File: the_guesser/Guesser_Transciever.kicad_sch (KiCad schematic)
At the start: 51 parts, among them J2 Conn_Coaxial, J3 BMI-S-209-F, U2 CC1101RGPR, U3 CC1190RGVR, U4 B39921B3728U410, X1 STDCRG2-27M

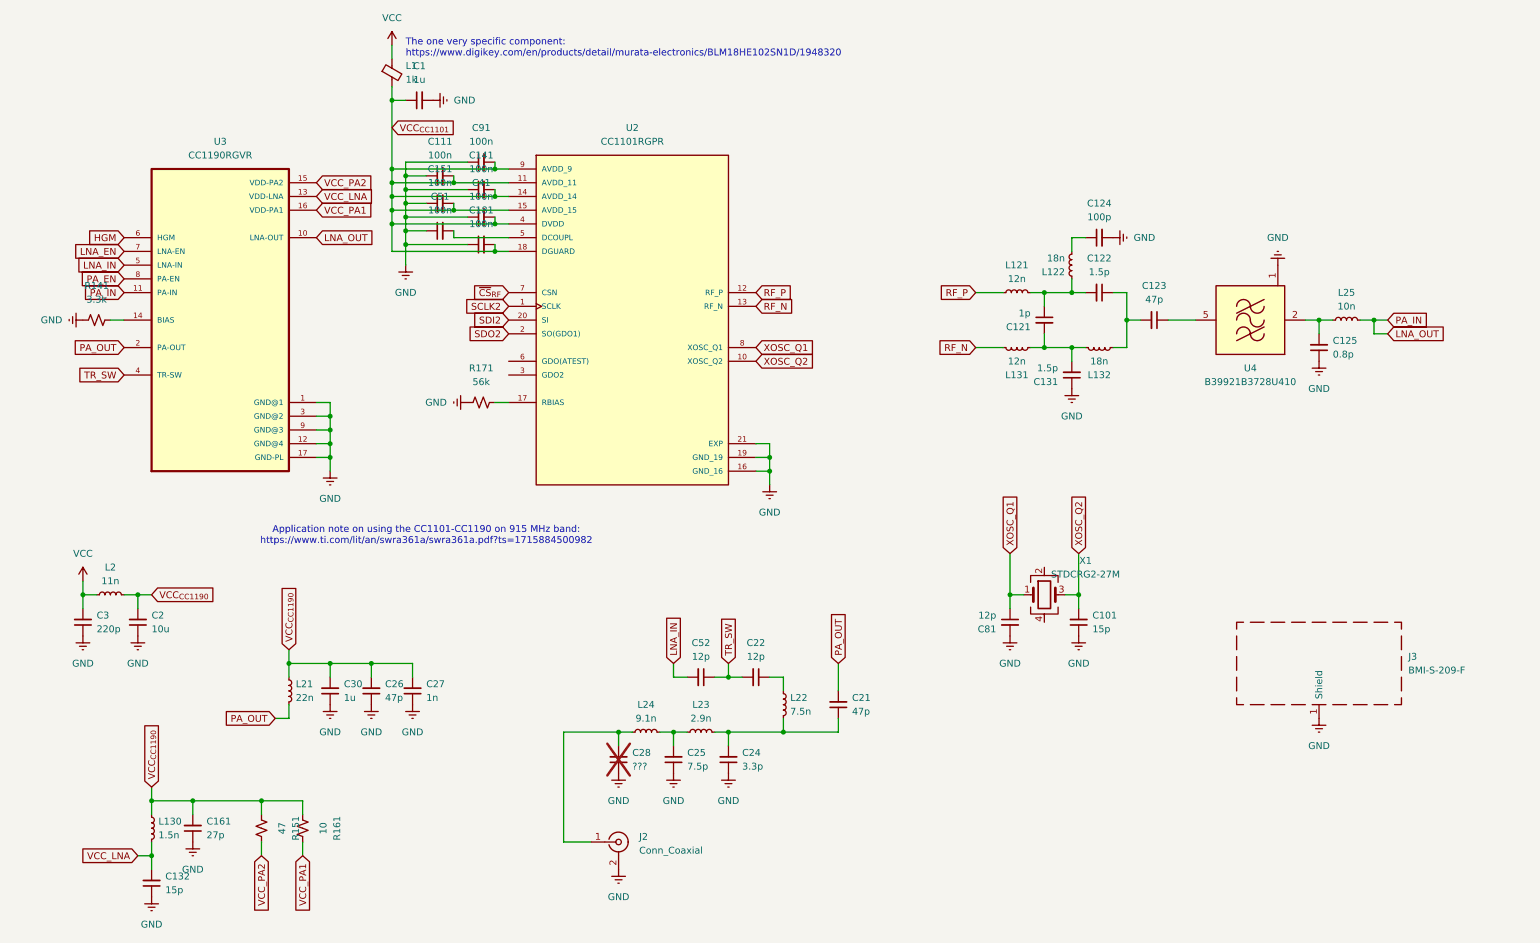
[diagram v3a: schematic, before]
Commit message: Finished Guesser sensor selection and started sensor routing
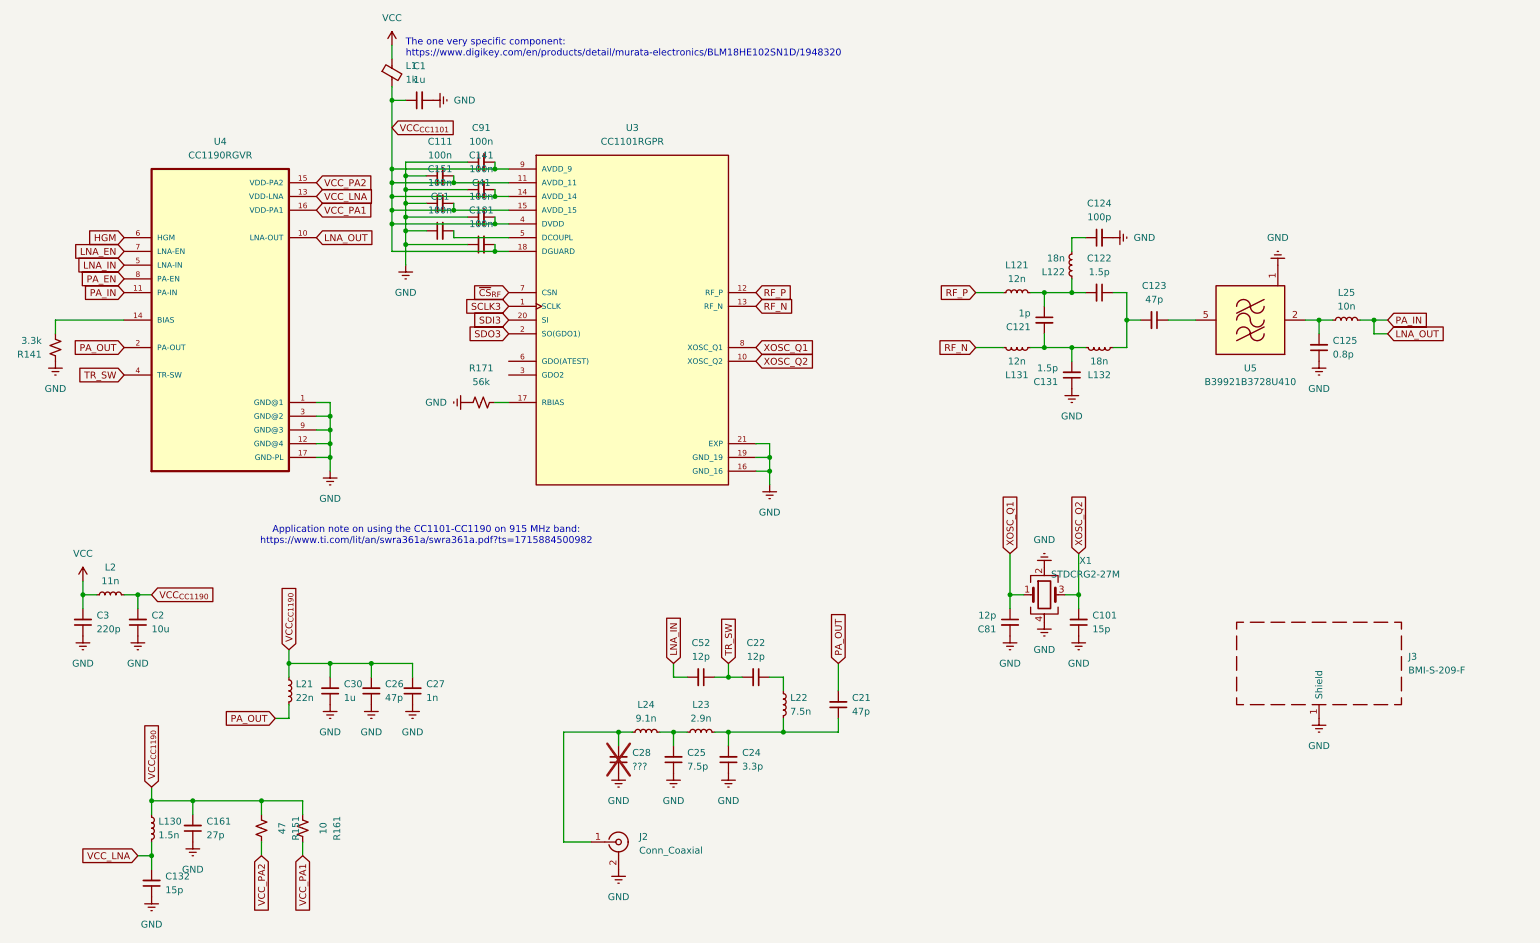
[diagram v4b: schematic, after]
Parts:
- U3: renamed from U2; footprint locals_but_working_PLEASE:QFN50P400X400X100-21N -> locals_but_working_PLEASE:CC1101RGPR
- U4: renamed from U3; footprint locals_but_working_PLEASE:QFN65P400X400X100-17N -> locals_but_working_PLEASE:CC1190RGVR
- renumbered U4 to U5
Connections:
- net GND: now also X1.2, X1.4
- net SCLK2 renamed SCLK3
- net SDI2 renamed SDI3
- net SDO2 renamed SDO3
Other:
- moved on the sheet: R141
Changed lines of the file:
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@@
 	(wire
 		(pts
+			(xy 20.32 76.2) (xy 33.02 76.2)
+		)
+		(stroke
+			(width 0)
+			(type default)
+		)
+	)
+	(wire
+		(pts
 			(xy 71.12 139.7) (xy 71.12 142.24)
 		)
@@
 	(wire
 		(pts
+			(xy 20.32 76.2) (xy 20.32 78.74)
+		)
+		(stroke
+			(width 0)
+			(type default)
+		)
+	)
+	(wire
+		(pts
 			(xy 85.09 57.15) (xy 96.52 57.15)
 		)
@@
 	(wire
 		(pts
-			(xy 30.48 76.2) (xy 33.02 76.2)
-		)
-		(stroke
-			(width 0)
-			(type default)
-		)
-	)
-	(wire
-		(pts
 			(xy 82.55 53.34) (xy 82.55 55.88)
 		)
@@
 		)
 	)
-	(global_label "SDO2"
+	(global_label "SDO3"
 		(shape input)
 		(at 104.14 78.74 180)
@@
 		)
 		(property "Intersheetrefs" "${INTERSHEET_REFS}"
-			(at 96.5586 78.74 0)
+			(at 96.1353 78.74 0)
 			(effects
 				(font
@@
 		)
 	)
-	(global_label "SCLK2"
+	(global_label "SCLK3"
 		(shape input)
 		(at 104.14 73.66 180)
@@
 		)
 		(property "Intersheetrefs" "${INTERSHEET_REFS}"
-			(at 96.3772 73.66 0)
+			(at 95.1677 73.66 0)
 			(effects
 				(font
@@
 		)
 	)
-	(global_label "SDI2"
+	(global_label "SDI3"
 		(shape input)
 		(at 104.14 76.2 180)
@@
 		)
 		(property "Intersheetrefs" "${INTERSHEET_REFS}"
-			(at 96.5586 76.2 0)
+			(at 96.861 76.2 0)
 			(effects
 				(font
@@
 	(symbol
 		(lib_id "power:Earth")
-		(at 25.4 76.2 270)
+		(at 20.32 83.82 0)
 		(unit 1)
 		(exclude_from_sim no)
@@
 		(fields_autoplaced yes)
 		(property "Reference" "#PWR021"
-			(at 19.05 76.2 0)
+			(at 20.32 90.17 0)
 			(effects
 				(font
@@
 		)
 		(property "Value" "GND"
-			(at 21.59 76.1999 90)
+			(at 20.32 88.9 0)
 			(effects
 				(font
 					(size 1.27 1.27)
 				)
-				(justify right)
 			)
 		)
 		(property "Footprint" ""
-			(at 25.4 76.2 0)
+			(at 20.32 83.82 0)
 			(effects
 				(font
@@
 		)
 		(property "Datasheet" "~"
-			(at 25.4 76.2 0)
+			(at 20.32 83.82 0)
 			(effects
 				(font
@@
 		)
 		(property "Description" "Power symbol creates a global label with name \"Earth\""
-			(at 25.4 76.2 0)
+			(at 20.32 83.82 0)
 			(effects
 				(font
@@
 		(dnp no)
 		(fields_autoplaced yes)
-		(property "Reference" "U3"
+		(property "Reference" "U4"
 			(at 50.8 43.18 0)
 			(effects
@@
 			)
 		)
-		(property "Footprint" "locals_but_working_PLEASE:QFN65P400X400X100-17N"
+		(property "Footprint" "locals_but_working_PLEASE:CC1190RGVR"
 			(at 50.8 76.2 0)
 			(effects
@@
 			(project "the_guesser"
 				(path "/473e3a2e-6c5e-4995-af4a-e4bf1449cab0/144203ce-f59d-4228-a9f3-243b499459b2"
-					(reference "U3")
+					(reference "U4")
 					(unit 1)
 				)
@@
 		(dnp no)
 		(fields_autoplaced yes)
-		(property "Reference" "U2"
+		(property "Reference" "U3"
 			(at 127 40.64 0)
 			(effects
@@
 			)
 		)
-		(property "Footprint" "locals_but_working_PLEASE:QFN50P400X400X100-21N"
+		(property "Footprint" "locals_but_working_PLEASE:CC1101RGPR"
 			(at 127 76.2 0)
 			(effects
@@
 			(project "the_guesser"
 				(path "/473e3a2e-6c5e-4995-af4a-e4bf1449cab0/144203ce-f59d-4228-a9f3-243b499459b2"
-					(reference "U2")
+					(reference "U3")
 					(unit 1)
 				)
@@
 		(dnp no)
 		(fields_autoplaced yes)
-		(property "Reference" "U4"
+		(property "Reference" "U5"
 			(at 241.3 85.09 0)
 			(effects
@@
 			(project "the_guesser"
 				(path "/473e3a2e-6c5e-4995-af4a-e4bf1449cab0/144203ce-f59d-4228-a9f3-243b499459b2"
-					(reference "U4")
+					(reference "U5")
 					(unit 1)
 				)
@@
 	(symbol
 		(lib_id "Device:R_Small_US")
-		(at 27.94 76.2 90)
+		(at 20.32 81.28 180)
 		(unit 1)
 		(exclude_from_sim no)
@@
 		(on_board yes)
 		(dnp no)
-		(fields_autoplaced yes)
 		(property "Reference" "R141"
-			(at 27.94 69.85 90)
+			(at 17.78 82.5501 0)
 			(effects
 				(font
 					(size 1.27 1.27)
 				)
+				(justify left)
 			)
 		)
 		(property "Value" "3.3k"
-			(at 27.94 72.39 90)
+			(at 17.78 80.0101 0)
 			(effects
 				(font
 					(size 1.27 1.27)
 				)
+				(justify left)
 			)
 		)
 		(property "Footprint" "Resistor_SMD:R_0603_1608Metric"
-			(at 27.94 76.2 0)
+			(at 20.32 81.28 0)
 			(effects
 				(font
@@
 		)
 		(property "Datasheet" "~"
-			(at 27.94 76.2 0)
+			(at 20.32 81.28 0)
 			(effects
 				(font
@@
 		)
 		(property "Description" "Resistor, small US symbol"
-			(at 27.94 76.2 0)
+			(at 20.32 81.28 0)
 			(effects
 				(font
@@
 	(symbol
 		(lib_id "power:Earth")
+		(at 203.2 132.08 0)
+		(unit 1)
+		(exclude_from_sim no)
+		(in_bom yes)
+		(on_board yes)
+		(dnp no)
+		(fields_autoplaced yes)
+		(property "Reference" "#PWR070"
+			(at 203.2 138.43 0)
+			(effects
+				(font
+					(size 1.27 1.27)
+				)
+				(hide yes)
+			)
+		)
+		(property "Value" "GND"
+			(at 203.2 137.16 0)
+			(effects
+				(font
+					(size 1.27 1.27)
+				)
+			)
+		)
+		(property "Footprint" ""
+			(at 203.2 132.08 0)
+			(effects
+				(font
+					(size 1.27 1.27)
+				)
+				(hide yes)
+			)
+		)
+		(property "Datasheet" "~"
+			(at 203.2 132.08 0)
+			(effects
+				(font
+					(size 1.27 1.27)
+				)
+				(hide yes)
+			)
+		)
+		(property "Description" "Power symbol creates a global label with name \"Earth\""
+			(at 203.2 132.08 0)
+			(effects
+				(font
+					(size 1.27 1.27)
+				)
+				(hide yes)
+			)
+		)
+		(pin "1"
+		)
+		(instances
+			(project "the_guesser"
+				(path "/473e3a2e-6c5e-4995-af4a-e4bf1449cab0/144203ce-f59d-4228-a9f3-243b499459b2"
+					(reference "#PWR070")
+					(unit 1)
+				)
+			)
+		)
+	)
+	(symbol
+		(lib_id "power:Earth")
 		(at 86.36 147.32 0)
 		(unit 1)
@@
 					(unit 1)
 				)
+			)
+		)
+	)
+	(symbol
+		(lib_id "power:Earth")
+		(at 203.2 121.92 180)
+		(unit 1)
+		(exclude_from_sim no)
+		(in_bom yes)
+		(on_board yes)
+		(dnp no)
+		(fields_autoplaced yes)
+		(property "Reference" "#PWR071"
+			(at 203.2 115.57 0)
+			(effects
+				(font
+					(size 1.27 1.27)
+				)
+				(hide yes)
+			)
+		)
+		(property "Value" "GND"
+			(at 203.2 116.84 0)
+			(effects
+				(font
+					(size 1.27 1.27)
+				)
+			)
+		)
+		(property "Footprint" ""
+			(at 203.2 121.92 0)
+			(effects
+				(font
+					(size 1.27 1.27)
+				)
+				(hide yes)
+			)
+		)
+		(property "Datasheet" "~"
+			(at 203.2 121.92 0)
+			(effects
+				(font
+					(size 1.27 1.27)
+				)
+				(hide yes)
+			)
+		)
+		(property "Description" "Power symbol creates a global label with name \"Earth\""
+			(at 203.2 121.92 0)
+			(effects
+				(font
+					(size 1.27 1.27)
+				)
+				(hide yes)
+			)
+		)
+		(pin "1"
+		)
+		(instances
+			(project "the_guesser"
+				(path "/473e3a2e-6c5e-4995-af4a-e4bf1449cab0/144203ce-f59d-4228-a9f3-243b499459b2"
+					(reference "#PWR071")
+					(unit 1)
+				)

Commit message: Routed USB and SPI buses
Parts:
- J2: footprint Connector_Coaxial:SMA_Amphenol_901-143_Horizontal -> Connector_Coaxial:SMA_Samtec_SMA-J-P-X-ST-EM1_EdgeMount
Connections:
- no-connect marks 0 -> 2
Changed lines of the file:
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@@
 		(color 0 0 0 0)
 	)
+	(no_connect
+		(at 104.14 86.36)
+	)
+	(no_connect
+		(at 104.14 83.82)
+	)
 	(wire
 		(pts
@@
 		(exclude_from_sim no)
 		(in_bom yes)
-		(on_board no)
+		(on_board yes)
 		(dnp no)
 		(fields_autoplaced yes)
@@
 			)
 		)
-		(property "Footprint" "Connector_Coaxial:SMA_Amphenol_901-143_Horizontal"
+		(property "Footprint" "Connector_Coaxial:SMA_Samtec_SMA-J-P-X-ST-EM1_EdgeMount"
 			(at 124.46 172.72 0)
 			(effects

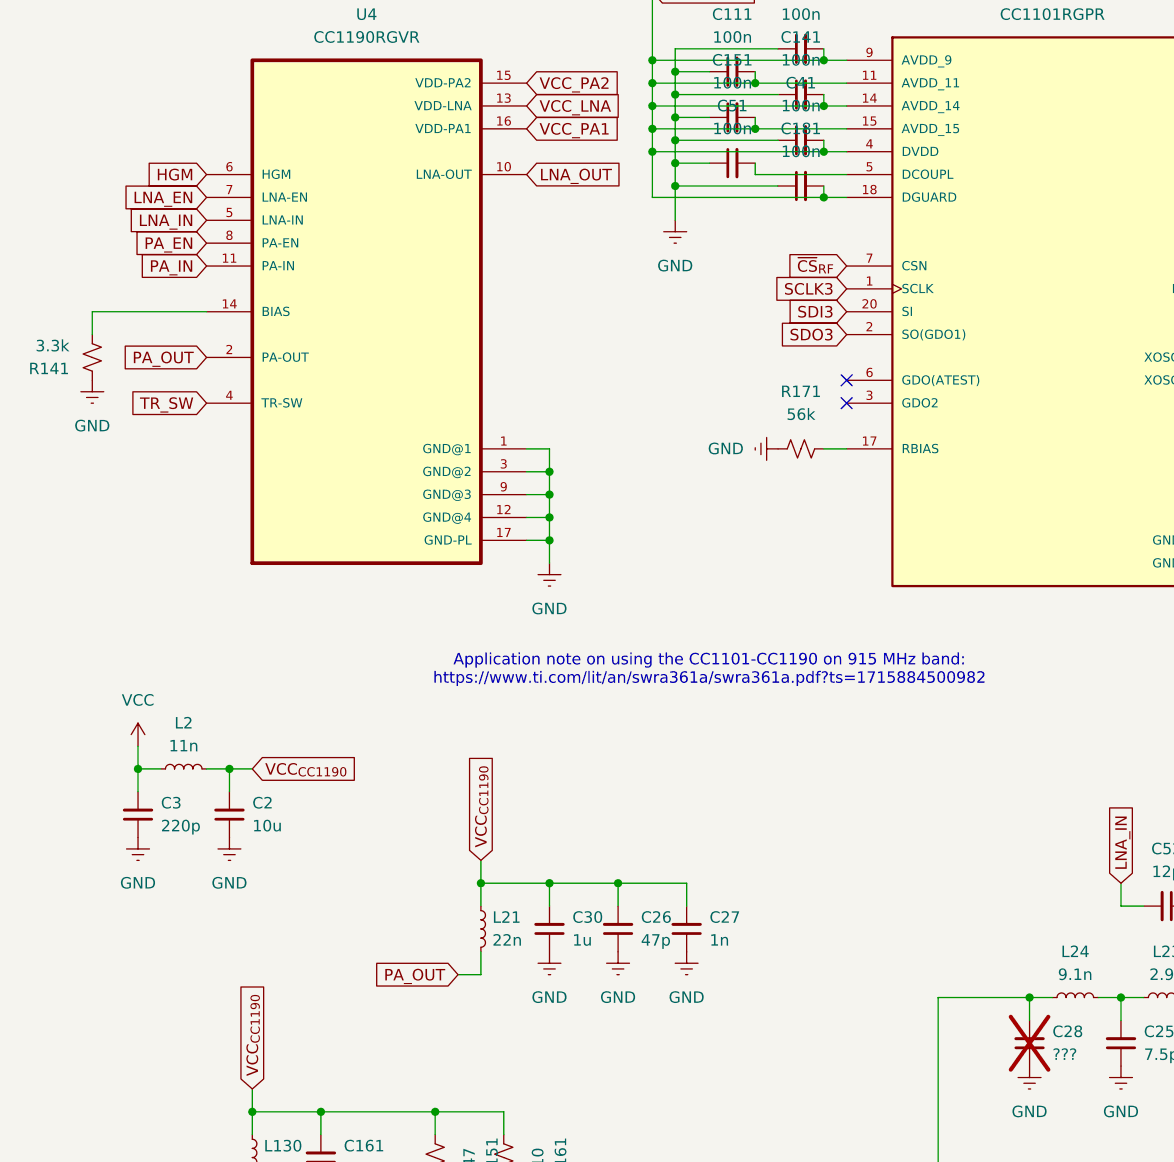
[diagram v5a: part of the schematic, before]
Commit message: Finished routing Guesser
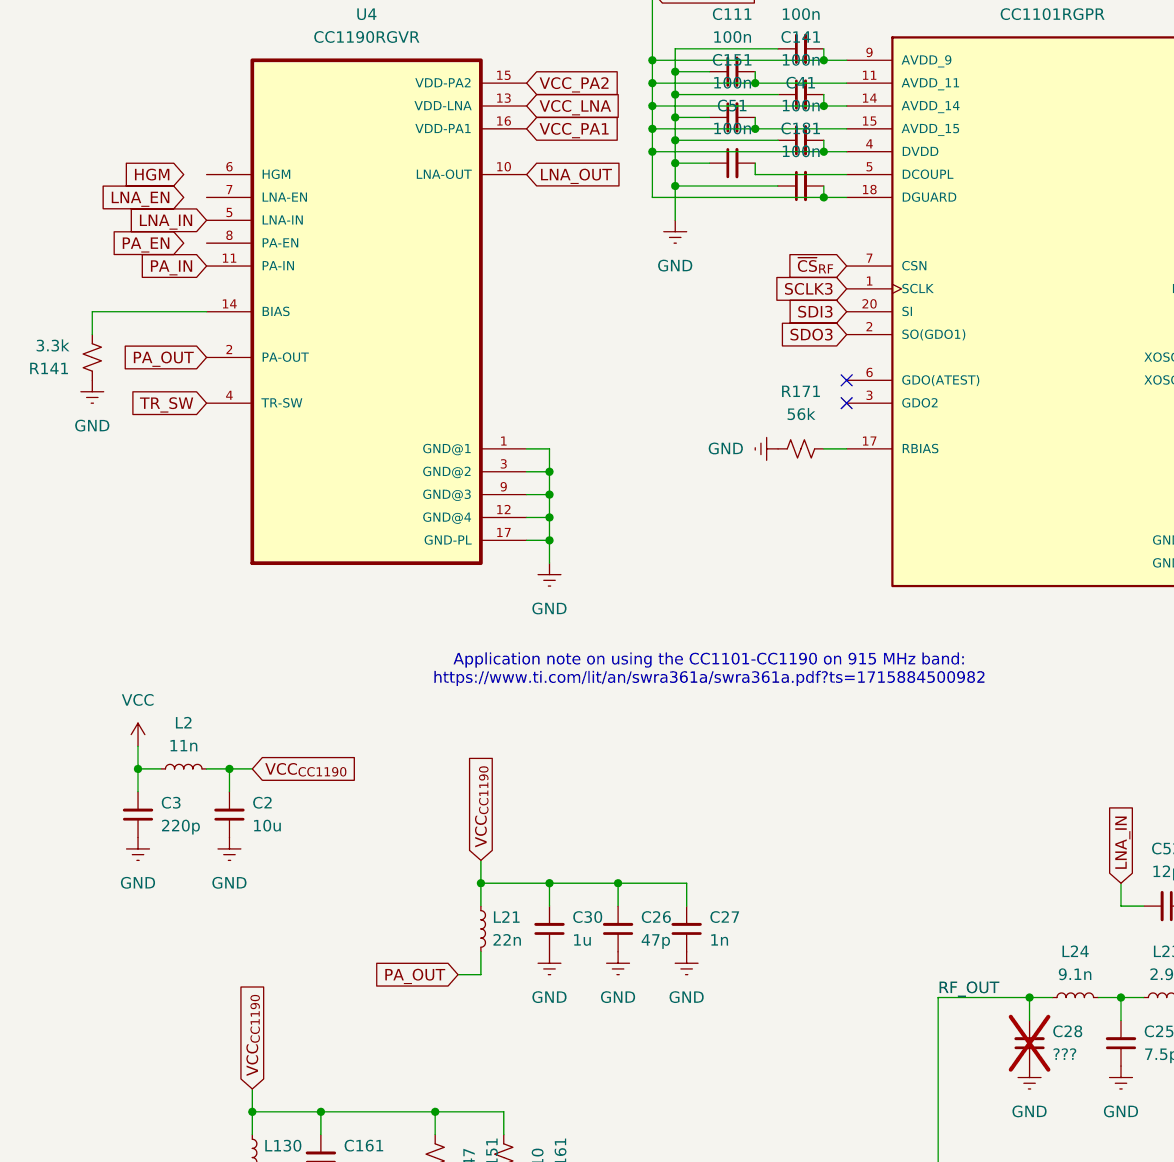
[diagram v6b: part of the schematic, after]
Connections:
- net HGM: no longer U4.6 (HGM)
- net LNA_EN: no longer U4.7 (LNA-EN)
- net PA_EN: no longer U4.8 (PA-EN)
- net RF_OUT: now reaches C28.2, J2.1 (In), L24.1
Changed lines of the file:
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@@
+		)
+	)
+	(label "RF_OUT"
+		(at 114.3 152.4 0)
+		(fields_autoplaced yes)
+		(effects
+			(font
+				(size 1.27 1.27)
+			)
+			(justify left bottom)
 		)
 	)
@@
 	(global_label "HGM"
 		(shape input)
-		(at 33.02 60.96 180)
-		(fields_autoplaced yes)
-		(effects
-			(font
-				(size 1.27 1.27)
-			)
-			(justify right)
-		)
-		(property "Intersheetrefs" "${INTERSHEET_REFS}"
-			(at 25.9829 60.96 0)
+		(at 30.48 60.96 180)
+		(fields_autoplaced yes)
+		(effects
+			(font
+				(size 1.27 1.27)
+			)
+			(justify right)
+		)
+		(property "Intersheetrefs" "${INTERSHEET_REFS}"
+			(at 23.4429 60.96 0)
 			(effects
 				(font
@@
 	(global_label "PA_EN"
 		(shape input)
-		(at 33.02 68.58 180)
-		(fields_autoplaced yes)
-		(effects
-			(font
-				(size 1.27 1.27)
-			)
-			(justify right)
-		)
-		(property "Intersheetrefs" "${INTERSHEET_REFS}"
-			(at 24.2291 68.58 0)
+		(at 30.48 68.58 180)
+		(fields_autoplaced yes)
+		(effects
+			(font
+				(size 1.27 1.27)
+			)
+			(justify right)
+		)
+		(property "Intersheetrefs" "${INTERSHEET_REFS}"
+			(at 21.6891 68.58 0)
 			(effects
 				(font
@@
 	(global_label "LNA_EN"
 		(shape input)
-		(at 33.02 63.5 180)
-		(fields_autoplaced yes)
-		(effects
-			(font
-				(size 1.27 1.27)
-			)
-			(justify right)
-		)
-		(property "Intersheetrefs" "${INTERSHEET_REFS}"
-			(at 23.1405 63.5 0)
-			(effects
-				(font
+		(at 30.48 63.5 180)
+		(fields_autoplaced yes)
+		(effects
+			(font
+				(size 1.27 1.27)
+			)
+			(justify right)
+		)
+		(property "Intersheetrefs" "${INTERSHEET_REFS}"
+			(at 20.6005 63.5 0)
+			(effects
+				(font
